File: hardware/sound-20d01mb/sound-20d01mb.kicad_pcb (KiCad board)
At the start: 2 copper layers, 199.4 x 69.9 mm, 123 parts, among them J1 USB_B, J10 Conn_01x02, J11 Conn_01x03, J12 Conn_01x04, J13 Conn_01x06, J14 Conn_01x03, J2 Conn_01x04, J3 Conn_02x08_Odd_Even, J4 Conn_02x04_Odd_Even, J5 Conn_01x06, J6 Conn_02x10_Odd_Even, J7 Conn_02x10_Odd_Even, J8 Conn_01x02, J9 Conn_01x02, SW1 SW_DIP_x02, U1 USBLC6-2SC6, U2 STM32F446RCTx, U3 PCM5142, U4 TPA3123D2, U5 PC817, U6 PC817, U7 ADP3338AKCZ-3.3RL7, U8 ADP3338AKCZ-3.3RL7, U9 L7805ABD2T-TR, X1 SM7745HEV-12.288M, Y1 32.768kHz, Y2 8MHz

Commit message: Updated PWP0024B
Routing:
- net PB5: track 19.5 -> 28.0 mm
- net GNDA: track 11.1 -> 19.1 mm

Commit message: Updated PCB
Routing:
- net +3V3: track 390.5 -> 480.3 mm, vias 15 -> 13
- net +5V: track 105.8 -> 185.2 mm, vias 0 -> 3
- net PC7: track 0.00 -> 34.5 mm, vias 0 -> 1
- net PA8: track 0.00 -> 30.2 mm, vias 0 -> 1
- net PC6: track 0.00 -> 29.3 mm, vias 0 -> 1
- net PC8: track 0.00 -> 29.1 mm, vias 0 -> 1
- net PD2: track 0.00 -> 28.0 mm, vias 0 -> 1
- net PA10: track 0.00 -> 24.9 mm, vias 0 -> 1
- net PC12: track 0.00 -> 22.8 mm, vias 0 -> 1
- net PC11: track 0.00 -> 22.8 mm, vias 0 -> 1
- net PA15: track 0.00 -> 22.7 mm, vias 0 -> 1
- net PC10: track 0.00 -> 22.2 mm, vias 0 -> 1
- net /Microcontroller Unit/NRST: track 42.8 -> 47.7 mm
- net /Microcontroller Unit/SWCLK: track 14.2 -> 17.8 mm
- net I2S_OSC_EN: track 33.2 -> 35.8 mm
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
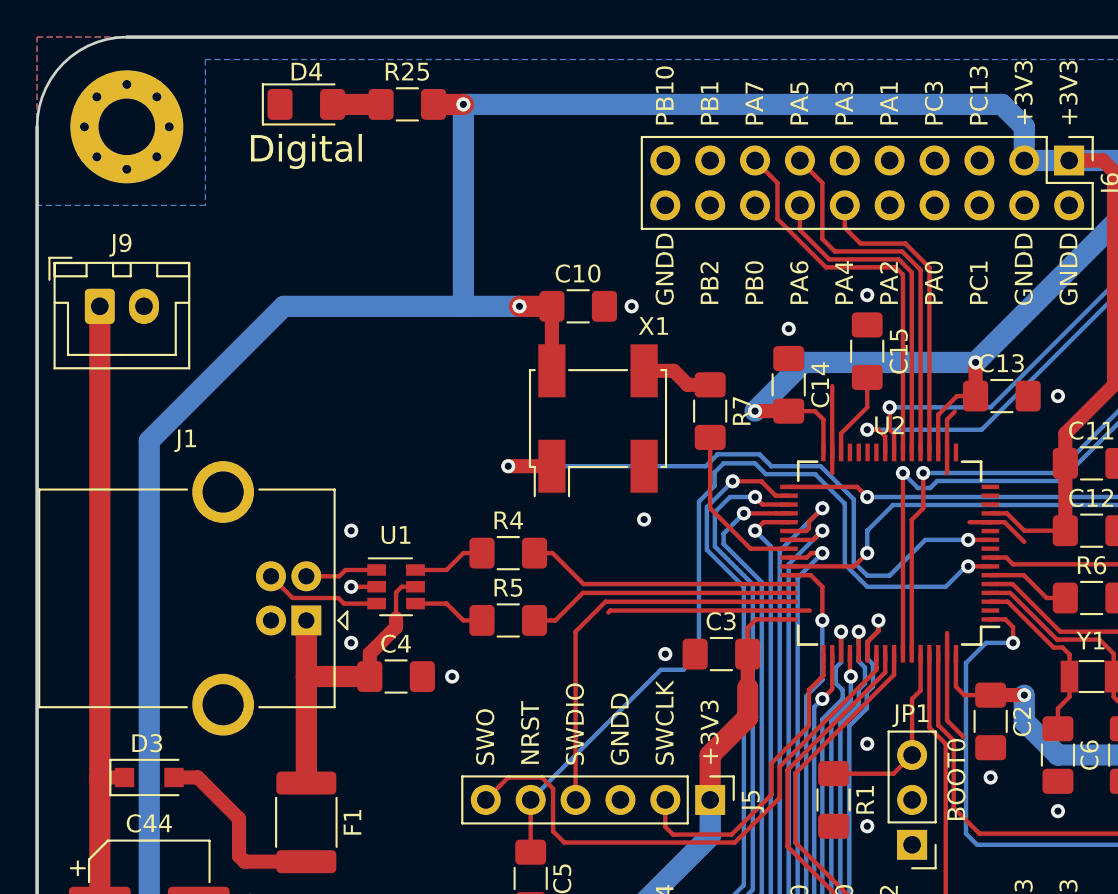
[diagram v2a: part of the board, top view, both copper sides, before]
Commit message: Added text EXT_5V
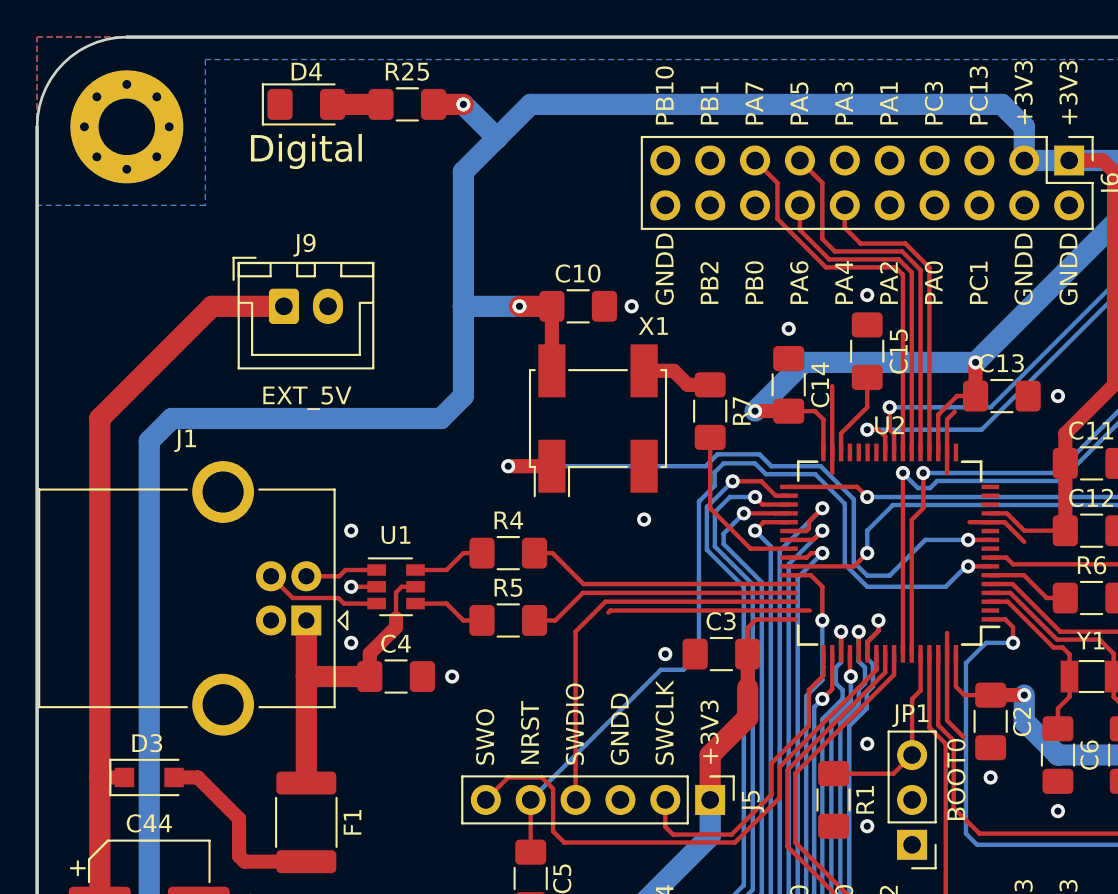
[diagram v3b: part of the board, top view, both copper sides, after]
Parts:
- moved J9 10.4 mm to (66.0, 72.4)
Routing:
- net +5V: track 185.2 -> 191.9 mm
- net +3V3: track 480.3 -> 483.8 mm
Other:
- board text added: "EXT_5V"
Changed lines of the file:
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@@
   (general
     (thickness 1.6)
-    (drawings 108)
-    (tracks 1155)
+    (drawings 109)
+    (tracks 1162)
     (zones 0)
     (modules 123)
@@
   )
   (setup
-    (last_trace_width 0.25)
+    (last_trace_width 1.2)
     (user_trace_width 0.45)
     (user_trace_width 0.8)
@@
   )
   (module Connector_JST:JST_XH_B02B-XH-A_1x02_P2.50mm_Vertical (layer F.Cu)
-    (at 55.62 72.39)
+    (at 66.04 72.39)
     (descr "JST XH series connector, B02B-XH-A (http://www.jst-mfg.com/product/pdf/eng/eXH.pdf), generated with kicad-footprint-generator")
     (tags "connector JST XH side entry")
@@
     )
   )
+  (gr_text EXT_5V (at 67.31 77.47) (layer F.SilkS)
+    (effects (font (size 1 1) (thickness 0.15)))
+  )
   (gr_text BOOT0 (at 104.14 101.6 90) (layer F.SilkS)
     (effects (font (size 1 1) (thickness 0.15)) (justify left))
@@
   (segment (start 59.69 113.03) (end 58.42 111.76) (width 1.2) (layer B.Cu) (net 1))
   (segment (start 60.96 114.3) (end 58.42 111.76) (width 1.2) (layer F.Cu) (net 1))
-  (segment (start 58.42 111.76) (end 58.42 80.01) (width 1.2) (layer B.Cu) (net 1))
-  (segment (start 58.42 80.01) (end 66.04 72.39) (width 1.2) (layer B.Cu) (net 1))
-  (segment (start 76.2 60.96) (end 76.2 72.39) (width 1.2) (layer B.Cu) (net 1))
-  (segment (start 66.04 72.39) (end 76.2 72.39) (width 1.2) (layer B.Cu) (net 1))
-  (segment (start 76.2 72.39) (end 79.375 72.39) (width 1.2) (layer B.Cu) (net 1))
   (segment (start 107.95 64.135) (end 107.95 62.23) (width 1.2) (layer B.Cu) (net 1))
-  (segment (start 106.68 60.96) (end 76.2 60.96) (width 1.2) (layer B.Cu) (net 1))
   (segment (start 107.95 62.23) (end 106.68 60.96) (width 1.2) (layer B.Cu) (net 1))
   (segment (start 107.95 95.885) (end 107.95 94.3975) (width 1.2) (layer B.Cu) (net 1))
@@
   (segment (start 113.03 76.835) (end 113.03 64.77) (width 0.8) (layer F.Cu) (net 1))
   (segment (start 112.395 64.135) (end 110.49 64.135) (width 0.8) (layer F.Cu) (net 1))
+  (segment (start 106.68 60.96) (end 80.01 60.96) (width 1.2) (layer B.Cu) (net 1))
+  (segment (start 78.105 62.865) (end 80.01 60.96) (width 1.2) (layer B.Cu) (net 1))
+  (segment (start 76.2 60.96) (end 78.105 62.865) (width 1.2) (layer B.Cu) (net 1))
+  (segment (start 76.2 72.39) (end 79.375 72.39) (width 1.2) (layer B.Cu) (net 1))
+  (segment (start 58.42 80.01) (end 59.69 78.74) (width 1.2) (layer B.Cu) (net 1))
+  (segment (start 58.42 111.76) (end 58.42 80.01) (width 1.2) (layer B.Cu) (net 1))
+  (segment (start 59.69 78.74) (end 74.93 78.74) (width 1.2) (layer B.Cu) (net 1))
+  (segment (start 74.93 78.74) (end 76.2 77.47) (width 1.2) (layer B.Cu) (net 1))
+  (segment (start 76.2 77.47) (end 76.2 72.39) (width 1.2) (layer B.Cu) (net 1))
+  (segment (start 76.2 64.77) (end 78.105 62.865) (width 1.2) (layer B.Cu) (net 1))
+  (segment (start 76.2 64.77) (end 76.2 72.39) (width 1.2) (layer B.Cu) (net 1))
   (via (at 85.725 72.39) (size 0.8) (drill 0.4) (layers F.Cu B.Cu) (net 2))
   (via (at 86.43 84.455) (size 0.8) (drill 0.4) (layers F.Cu B.Cu) (net 2))
@@
   (segment (start 57.02 99.06) (end 55.62 99.06) (width 0.8) (layer F.Cu) (net 31))
   (segment (start 55.62 106.045) (end 55.62 99.06) (width 1.2) (layer F.Cu) (net 31))
-  (segment (start 55.62 99.06) (end 55.62 72.39) (width 1.2) (layer F.Cu) (net 31))
   (segment (start 149.225 118.85) (end 140.23 118.85) (width 1.2) (layer F.Cu) (net 31))
   (segment (start 137.16 121.92) (end 125.73 121.92) (width 1.2) (layer F.Cu) (net 31))
@@
   (segment (start 108.585 120.65) (end 112.395 124.46) (width 1.2) (layer B.Cu) (net 31))
   (segment (start 63.24 120.65) (end 108.585 120.65) (width 1.2) (layer B.Cu) (net 31))
+  (segment (start 61.97 72.39) (end 55.62 78.74) (width 1.2) (layer F.Cu) (net 31))
+  (segment (start 66.04 72.39) (end 61.97 72.39) (width 1.2) (layer F.Cu) (net 31))
+  (segment (start 55.62 99.06) (end 55.62 78.74) (width 1.2) (layer F.Cu) (net 31))
   (via (at 227.33 60.96) (size 0.8) (drill 0.4) (layers F.Cu B.Cu) (net 32))
   (via (at 194.945 74.295) (size 0.8) (drill 0.4) (layers F.Cu B.Cu) (net 32))

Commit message: All connections are connected
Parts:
- moved C13 3.31 mm to (104.6, 74.9), turned to 90 degrees
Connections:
- J6 pad 10: PA2 -> PC13
- J6 pad 5: PC13 -> PA0
- J6 pad 6: PC1 -> PA1
- J6 pad 7: PC3 -> PA2
- J6 pad 8: PA0 -> PC3
- J6 pad 9: PA1 -> PC1
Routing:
- net PC1: track 0.00 -> 31.3 mm
- net PC13: track 0.00 -> 31.0 mm
- net PB1: track 0.00 -> 29.5 mm, vias 0 -> 1
- net PB2: track 0.00 -> 28.6 mm, vias 0 -> 1
- net PB10: track 0.00 -> 27.2 mm, vias 0 -> 1
- net PC3: track 0.00 -> 25.6 mm
- net PA3: track 0.00 -> 24.5 mm
- net PA0: track 0.00 -> 24.2 mm
- net PB0: track 0.00 -> 24.2 mm, vias 0 -> 1
- net PA1: track 0.00 -> 23.2 mm
- net PA2: track 0.00 -> 23.0 mm
- net /Amplifier/~SHUTDOWN: track 48.0 -> 45.5 mm
- net PC7: track 34.5 -> 32.5 mm
- net /DAC/DAC_CK: track 47.3 -> 48.9 mm
- net /Microcontroller Unit/NRST: track 47.7 -> 46.2 mm
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
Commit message: Updated PCB
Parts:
- moved R1 17.5 mm to (113.7, 106.0)
- moved JP1 5.24 mm to (106.7, 101.6), turned to 270 degrees
- moved C5 1.27 mm to (80.0, 106.0)
- moved J5 1.27 mm to (90.2, 101.6)
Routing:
- net /Microcontroller Unit/SWO: track 31.6 -> 46.0 mm
- net /Microcontroller Unit/BOOT0: track 10.8 -> 23.0 mm, vias 0 -> 1
- net PD2: track 28.0 -> 22.5 mm, vias 1 -> 0
- net PB4: track 24.6 -> 20.0 mm
- net PB5: track 28.7 -> 24.2 mm
- net PC10: track 22.2 -> 18.5 mm, vias 1 -> 0
- net PC12: track 22.8 -> 19.2 mm, vias 1 -> 0
- net /Microcontroller Unit/SWCLK: track 17.8 -> 21.5 mm
- net /Microcontroller Unit/NRST: track 46.2 -> 47.5 mm
- net /Microcontroller Unit/SWDIO: track 22.3 -> 23.6 mm
- net PA15: track 22.7 -> 21.7 mm, vias 1 -> 0
- net PC11: track 22.8 -> 21.9 mm, vias 1 -> 0
- net PB14: track 33.9 -> 34.6 mm
- net GNDD: vias 32 -> 34
- net GNDA: vias 34 -> 35

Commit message: Updated PCB
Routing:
- net /Amplifier/MUTE: track 47.0 -> 45.6 mm
- net GNDD: track 33.6 -> 33.3 mm, vias 34 -> 36
- net GNDA: vias 35 -> 37
